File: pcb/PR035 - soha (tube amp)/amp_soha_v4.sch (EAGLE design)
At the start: 56 parts, among them IC1 NE5532, IC2 7812, IC3 7912, Q1 J113, Q2 J113, Q3 J113, Q4 J113

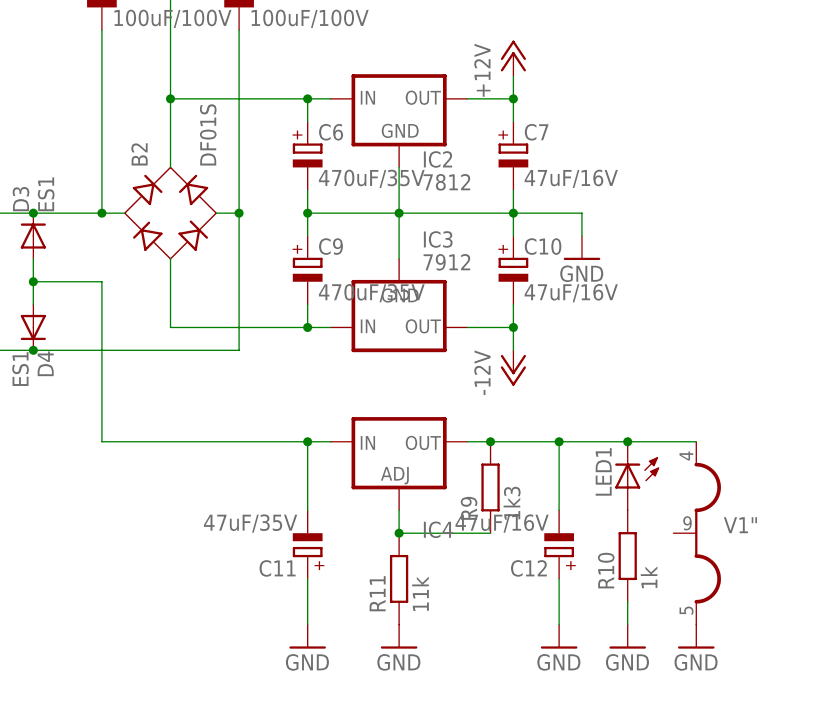
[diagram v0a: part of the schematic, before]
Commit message: 
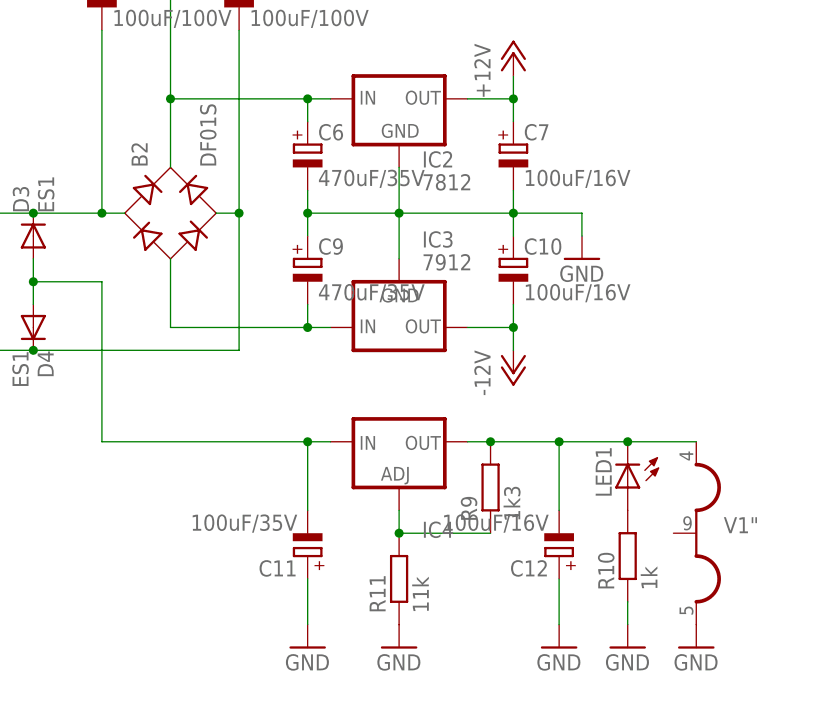
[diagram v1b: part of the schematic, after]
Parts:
- C10, C12, C7: value 47uF/16V -> 100uF/16V
- C11: value 47uF/35V -> 100uF/35V
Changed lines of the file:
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@@
 <?xml version="1.0" encoding="utf-8"?>
 <!DOCTYPE eagle SYSTEM "eagle.dtd">
-<eagle version="6.4">
+<eagle version="6.5.0">
 <drawing>
 <settings>
@@
 <part name="D3" library="amp_soha" deviceset="ES1" device=""/>
 <part name="D4" library="amp_soha" deviceset="ES1" device=""/>
-<part name="C11" library="amp_soha" deviceset="CPOL-EU" device="E2.5-6" value="47uF/35V"/>
+<part name="C11" library="amp_soha" deviceset="CPOL-EU" device="E2.5-6" value="100uF/35V"/>
 <part name="R9" library="amp_soha" deviceset="R-EU_" device="" value="1k3"/>
 <part name="R11" library="amp_soha" deviceset="R-EU_" device="" value="11k"/>
-<part name="C12" library="amp_soha" deviceset="CPOL-EU" device="E2.5-6" value="47uF/16V"/>
+<part name="C12" library="amp_soha" deviceset="CPOL-EU" device="E2.5-6" value="100uF/16V"/>
 <part name="R10" library="amp_soha" deviceset="R-EU_" device="" value="1k"/>
 <part name="LED1" library="amp_soha" deviceset="LED" device="5MM"/>
@@
 <part name="C6" library="amp_soha" deviceset="CPOL-EU" device="E5-10,5" value="470uF/35V"/>
 <part name="C9" library="amp_soha" deviceset="CPOL-EU" device="E5-10,5" value="470uF/35V"/>
-<part name="C10" library="amp_soha" deviceset="CPOL-EU" device="E2.5-6" value="47uF/16V"/>
-<part name="C7" library="amp_soha" deviceset="CPOL-EU" device="E2.5-6" value="47uF/16V"/>
+<part name="C10" library="amp_soha" deviceset="CPOL-EU" device="E2.5-6" value="100uF/16V"/>
+<part name="C7" library="amp_soha" deviceset="CPOL-EU" device="E2.5-6" value="100uF/16V"/>
 <part name="P+1" library="amp_soha" deviceset="+12V" device=""/>
 <part name="P-1" library="amp_soha" deviceset="-12V" device=""/>
